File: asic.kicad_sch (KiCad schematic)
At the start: 39 parts, among them U1 50MHz, U13 ADP171AUJ-R7, U2 TXB0104RGYR

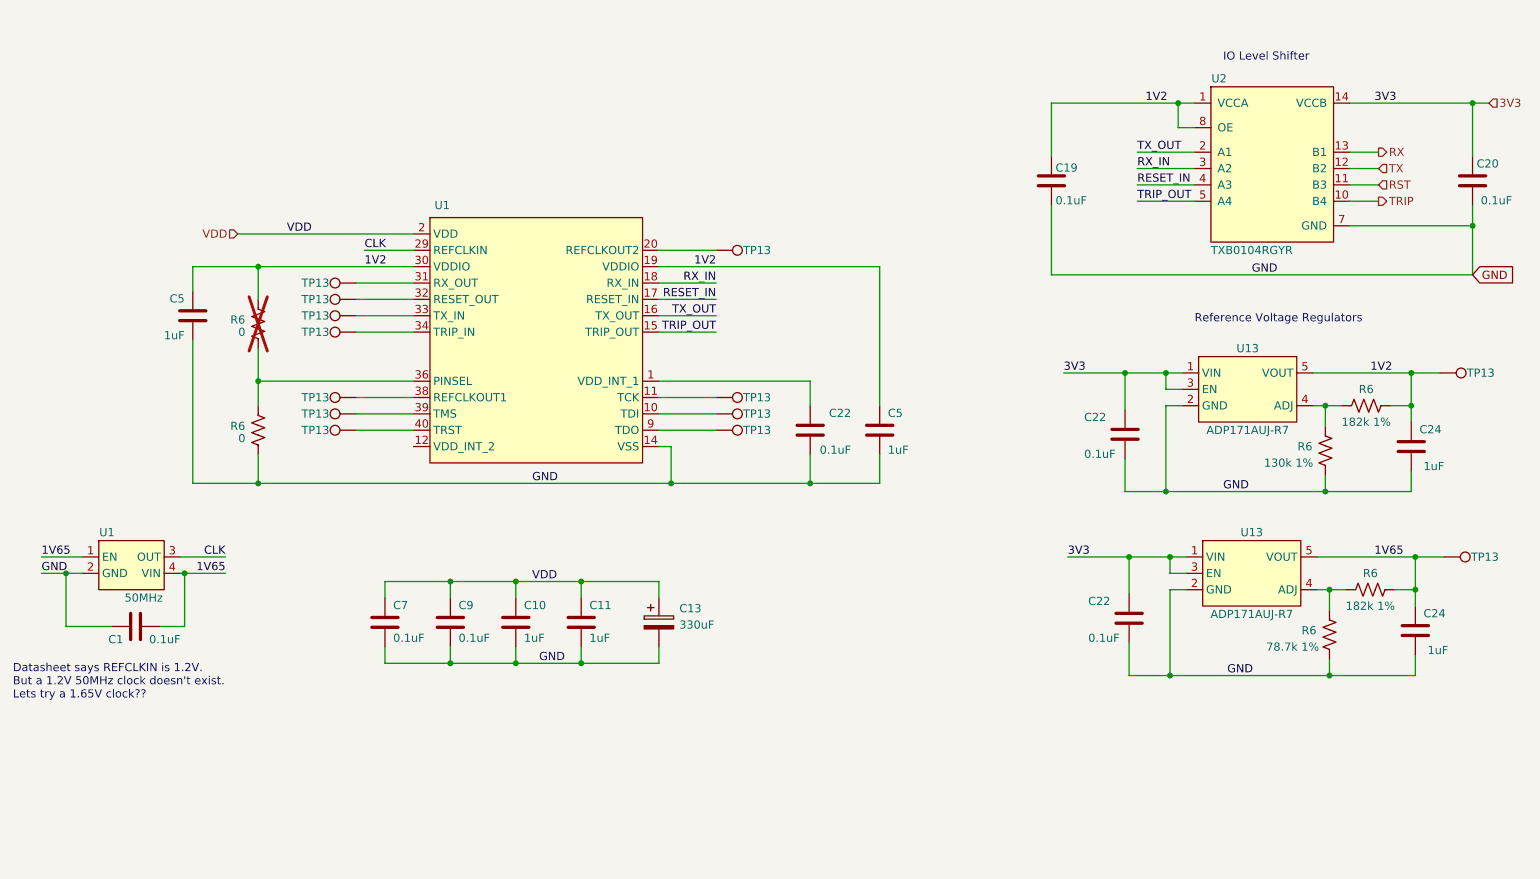
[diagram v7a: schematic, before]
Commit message: Switching to 1.2V Oscillator for #3 Switch the level shifter for #4
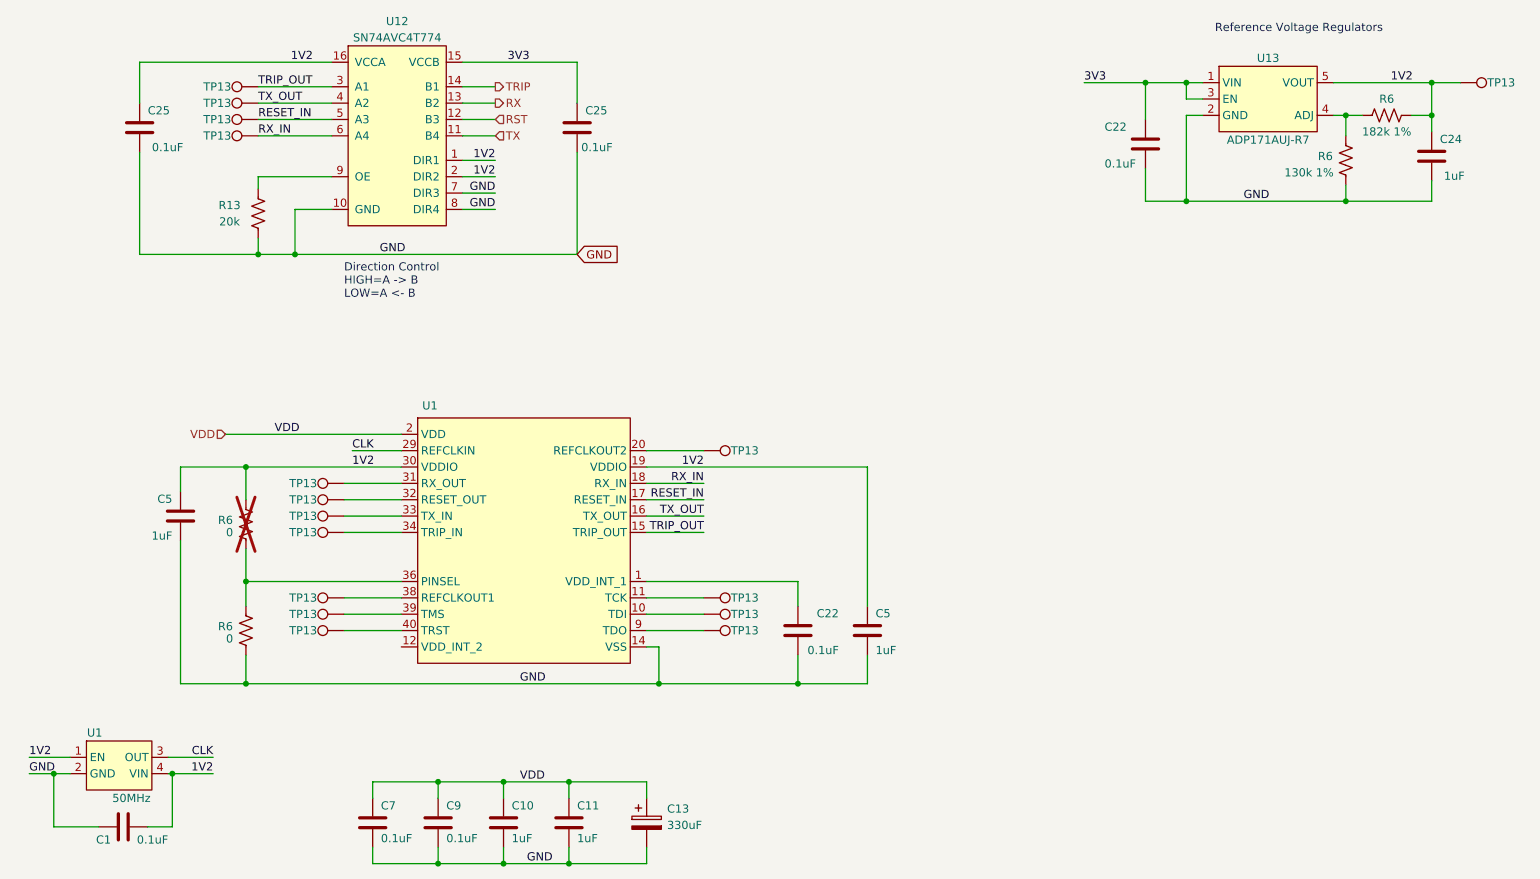
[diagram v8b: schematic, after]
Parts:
- removed C19, C20, C22: 0.1uF, Capacitor_SMD:C_0402_1005Metric, symbol Device:C
- removed C24: 1uF, Capacitor_SMD:C_0402_1005Metric, symbol Device:C
- removed R6: 182k 1%, Resistor_SMD:R_0402_1005Metric, symbol Device:R_US
- removed R6: 78.7k 1%, Resistor_SMD:R_0402_1005Metric, symbol Device:R_US
- removed TP13: TestPoint, TestPoint:TestPoint_Pad_D1.0mm, symbol Connector:TestPoint
- removed U13: ADP171AUJ-R7, Package_TO_SOT_SMD:TSOT-23-5, symbol bitaxe:ADP171AUJ-R7
- removed U2: TXB0104RGYR, blockaxe:TXB0104, symbol bitaxe:TXB0104RGYR
- added C25 (x2): 311-3342-1-ND, Capacitor_SMD:C_0402_1005Metric, symbol Device:C
- added R13: 20k, Resistor_SMD:R_0402_1005Metric, symbol Device:R_US
- added TP13 (x4): TestPoint, TestPoint:TestPoint_Pad_D1.0mm, symbol Connector:TestPoint
- added U12: SN74AVC4T774, Package_SO:TSSOP-16_4.4x5mm_P0.65mm, symbol bitaxe:SN74AVC4T774
- U1: DK XC2889CT-ND -> (none); LCSC (none) -> C5137267; PARTNO ECS-3225MV-500-CN-TR -> SX3M50.000E20F30THN
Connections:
- net 1V65 is gone; now on net 1V2: C1.2, U1.1 (EN), U1.4 (VIN)
- net 1V2: now also C25.1, U12.1 (DIR1), U12.16 (VCCA), U12.2 (DIR2)
- net 3V3: now also C25.1, U12.15 (VCCB)
- net GND: now also C25.2, C25.2, R13.1, U12.10 (GND), U12.7 (DIR3), U12.8 (DIR4)
- net RESET_IN: now also TP13.1, U12.5 (A3)
- net RST: now also U12.12 (B3)
- net RX: now also U12.13 (B2)
- net RX_IN: now also TP13.1, U12.6 (A4)
- net TRIP: now also U12.14 (B1)
- net TRIP_OUT: now also TP13.1, U12.3 (A1)
- net TX: now also U12.11 (B4)
- net TX_OUT: now also TP13.1, U12.4 (A2)
- new net: R13.2, U12.9 (OE)
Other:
- note added: "Direction Control HIGH=A -> B LOW=A <- B"
- note removed: "Datasheet says REFCLKIN is 1.2V. But a 1.2V 50MHz clock doesn't exist. Lets try a 1.65V clock??"
- note removed: "IO Level Shifter"
- moved on the sheet: C1, C10, C11, C13, C22, C24, C5, C7, C9, R6, TP13, U1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
